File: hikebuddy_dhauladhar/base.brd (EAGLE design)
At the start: 75 x 40 mm, 119 parts, among them J1 MF-CON-MICROUSB-RIGHT, J2 GPS Port, J5 SOLDER_PAD_2, J9 47352-1001, U1 LTC3586EUFE-1#PBF, U2 MAX17260SETD+, U3 MF-DSC-SOT233-MMBT3904, U4 MF-DSC-SOT233-MMBT3904, U5 DRV2605LTDGSRQ1, U7 LSM303CTR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

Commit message: pulled up fault and EN to V_REG to fix startup bug
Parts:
- added C20: 1uF, MF_Passives:C0603
- added R16: 10K, MF_Passives:R0603
- moved C24 0.05 mm to (10.8, 19.2)
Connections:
- new net N$24: C20.P$2, R16.P$2, U1.18, U1.38
- net GND: now also C20.P$1
- net V_REG: now also R16.P$1; no longer U1.18
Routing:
- net N$24: track 0.00 -> 38.6 mm, vias 0 -> 2
- net EN_SDC: track 15.6 -> 17.0 mm
- net EN_GPS: track 14.0 -> 15.1 mm
- net SW4: track 72.1 -> 71.6 mm
- net SW3: track 59.2 -> 58.6 mm
- net VCC: track 235.5 -> 235.0 mm

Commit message: replace lsm303 with bmx160
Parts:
- removed C39: 10uF, SparkFun-Capacitors:C0603
- removed C40: 0.1uF, SparkFun-Capacitors:C0603
- removed R39: 750K, SparkFun-Resistors:R0603
- removed R44: 560K, SparkFun-Resistors:R0603
- removed R45: 100K, SparkFun-Resistors:R0603
- removed U7: LSM303CTR, LSM303CTR:LGA-12
- removed U9: LTC6991CDCB#TRMPBF, LTC6991CS6TRMPBF:DFN
- added C21: 10uF, SparkFun-Capacitors:C0603
- added U6: BMX160, BMX160:PQFN50P250X300X100-14N
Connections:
- removed net N$23: C40.2, U7.5
- removed net N$35: U$5.EXTCOMIN, U9.6
- removed net N$40: R39.1, U9.3
- removed net N$42: R44.2, R45.1, U9.2
- net ACCL1: now also J8.6; no longer U7.7
- net ACCL2: now also U6.4; no longer U7.12
- net ESP_FLASH: no longer J8.6
- net GND: now also C21.2, U6.1, U6.2, U6.3, U6.6, U6.7; no longer C39.2, C40.1, R39.2, R45.2, U7.6, U7.8, U9.4, U9.5, U9.7
- net I2C_SCL: now also U6.13; no longer U7.1
- net I2C_SDA: now also U6.14; no longer U7.4
- net MAGDRDY: now also U$5.EXTCOMIN; no longer U7.11
- net VCC: now also C21.1, U6.12, U6.5, U6.8; no longer C39.1, U7.10, U7.2, U7.3, U7.9
- net V_LCD: no longer R44.1, U9.1
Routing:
- net GND: track 505.3 -> 497.5 mm, vias 95 -> 94
- net N$42: track 5.21 -> 0.00 mm, vias 2 -> 0
- net VCC: track 235.0 -> 230.8 mm
- net N$35: track 4.03 -> 0.00 mm, vias 2 -> 0
- net MAGDRDY: track 50.8 -> 54.3 mm, vias 3 -> 5
- net ESP_FLASH: track 70.9 -> 67.4 mm
- net N$23: track 2.74 -> 0.00 mm, vias 1 -> 0
- net I2C_SDA: track 112.9 -> 111.2 mm
- net I2C_SCL: track 111.3 -> 109.8 mm
- net V_LCD: track 57.9 -> 56.6 mm
- net N$40: track 1.26 -> 0.00 mm
- net ACCL2: track 44.1 -> 43.0 mm
- net ACCL1: track 39.7 -> 39.2 mm
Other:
- board text added: "IO13"
- board text added: "IO14"
- board text added: "IO15"
- board text added: "IO33"
- board text removed: "GPIO0/ FLASH"
- board text removed: "GPIO13"
- board text removed: "GPIO14"
- board text removed: "GPIO15"

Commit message: fixed power, routed bmx160, changed and routed buttons; cs_v2_non_macrofab
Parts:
- S1, S2, S3, S4: value B3U-3000P -> EVQ-P4HB3B; device B3U-3000P:SW_B3U-3000P -> EVQ-P4HB3B:SW_EVQ-P4HB3B
- moved S4 14.7 mm to (53.7, 38.3)
- moved S2 13.5 mm to (39.5, 38.3)
- moved R33 1.96 mm to (54.4, 38.9), flipped to the top, turned to 0 degrees
- moved U6 1.00 mm to (45.0, 20.0)
- moved C21 0.99 mm to (44.8, 17.6)
- moved S1 0.83 mm to (53.7, 1.70)
- moved S3 0.71 mm to (25.6, 38.3)
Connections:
- net GND: now also S1.2, S1.3, S1.4, S2.2, S2.3, S2.4, S3.2, S3.3, S3.4, S4.2, S4.3, S4.4; no longer S1.1, S2.1, S3.1, S4.1
- net SW1: now also S1.1; no longer S1.2
- net SW2: now also S4.1; no longer S2.2
- net SW3: now also S3.1; no longer S3.2
- net SW4: now also S2.1; no longer S4.2
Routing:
- net GND: track 497.5 -> 526.5 mm, vias 94 -> 95
- net MAGDRDY: track 54.3 -> 41.4 mm, vias 5 -> 3
- net VCC: track 230.8 -> 241.6 mm
- net ESP_FLASH: track 67.4 -> 58.1 mm, vias 5 -> 3
- net SW3: track 58.6 -> 64.5 mm
- net ACCL2: track 43.0 -> 37.2 mm, vias 3 -> 1
- net SW2: track 89.0 -> 84.0 mm, vias 2 -> 3
- net I2C_SDA: track 111.2 -> 115.6 mm
- net ACCL1: track 39.2 -> 35.0 mm, vias 3 -> 2
- net I2C_SCL: track 109.8 -> 113.4 mm
- net SW1: track 68.1 -> 71.5 mm
- net N$33: track 27.5 -> 29.3 mm
- net SW4: track 71.6 -> 69.9 mm
- net V_LCD: track 56.6 -> 55.6 mm
- net N$32: track 27.9 -> 28.8 mm
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
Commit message: cs_v2_macrofab_sdc_version
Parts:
- removed J9: 47352-1001, 47352-1001:MOLEX_47352-1001
- added SD1: MF-MICROSD, MF_Connectors:MF-MICROSD
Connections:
- removed net N$19: J9.8
- removed net N$45: J9.1
- net 3V3_SDC: now also SD1.PIN4; no longer J9.4
- net GND: now also SD1.G0, SD1.G1, SD1.PIN6; no longer J9.6, J9.S1, J9.S2, J9.S3, J9.S4
- net SD_CLK: now also SD1.PIN5; no longer J9.5
- net SD_CS: now also SD1.PIN2; no longer J9.2
- net SD_MISO: now also SD1.PIN7; no longer J9.7
- net SD_MOSI: now also SD1.PIN3; no longer J9.3
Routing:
- net GND: track 526.5 -> 520.2 mm, vias 95 -> 94
- net SD_MISO: track 24.9 -> 23.1 mm
- net SD_CS: track 25.1 -> 23.5 mm
- net ESP_FLASH: track 58.1 -> 56.5 mm
- net SD_MOSI: track 22.9 -> 21.6 mm
- net 3V3_SDC: track 28.7 -> 27.4 mm
- net SD_CLK: track 26.5 -> 25.2 mm
- net EN_SDC: track 17.0 -> 18.1 mm
- net VCC: track 241.6 -> 242.5 mm

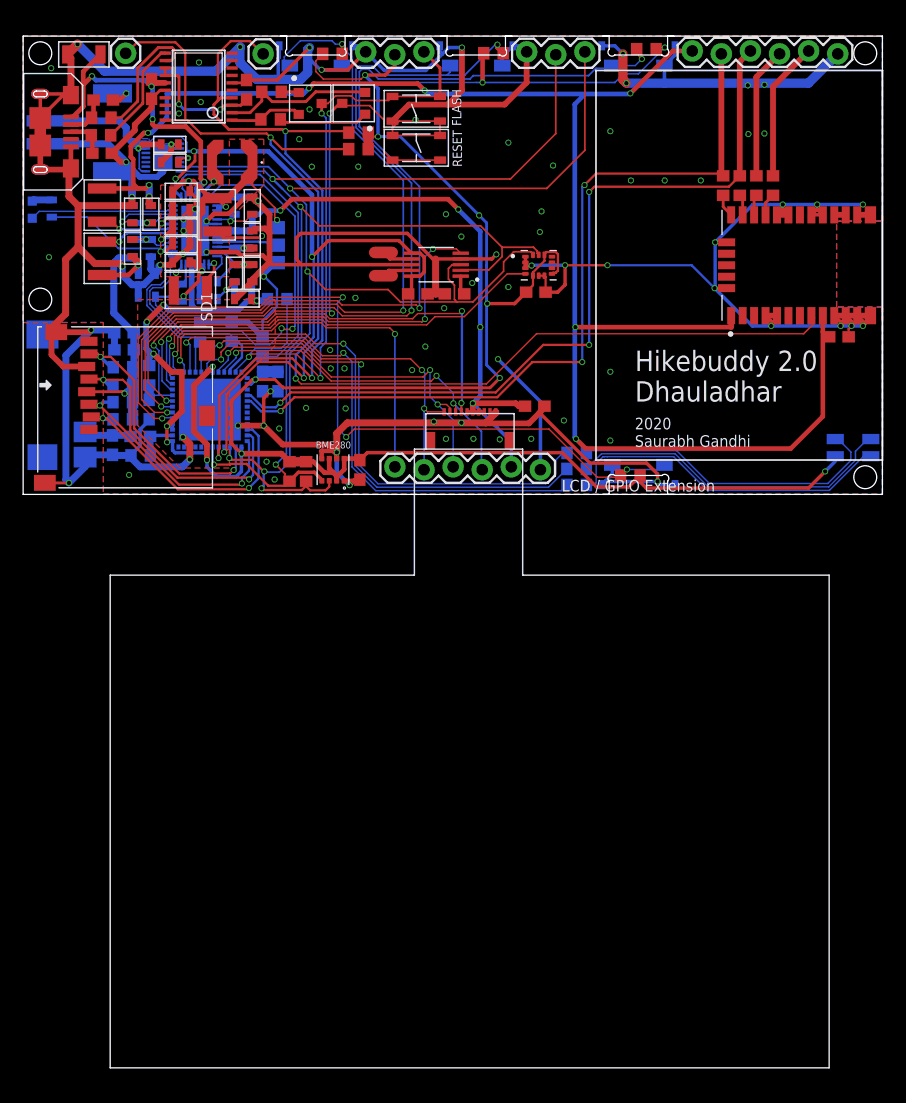
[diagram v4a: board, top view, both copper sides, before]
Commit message: reassigned input-only pins
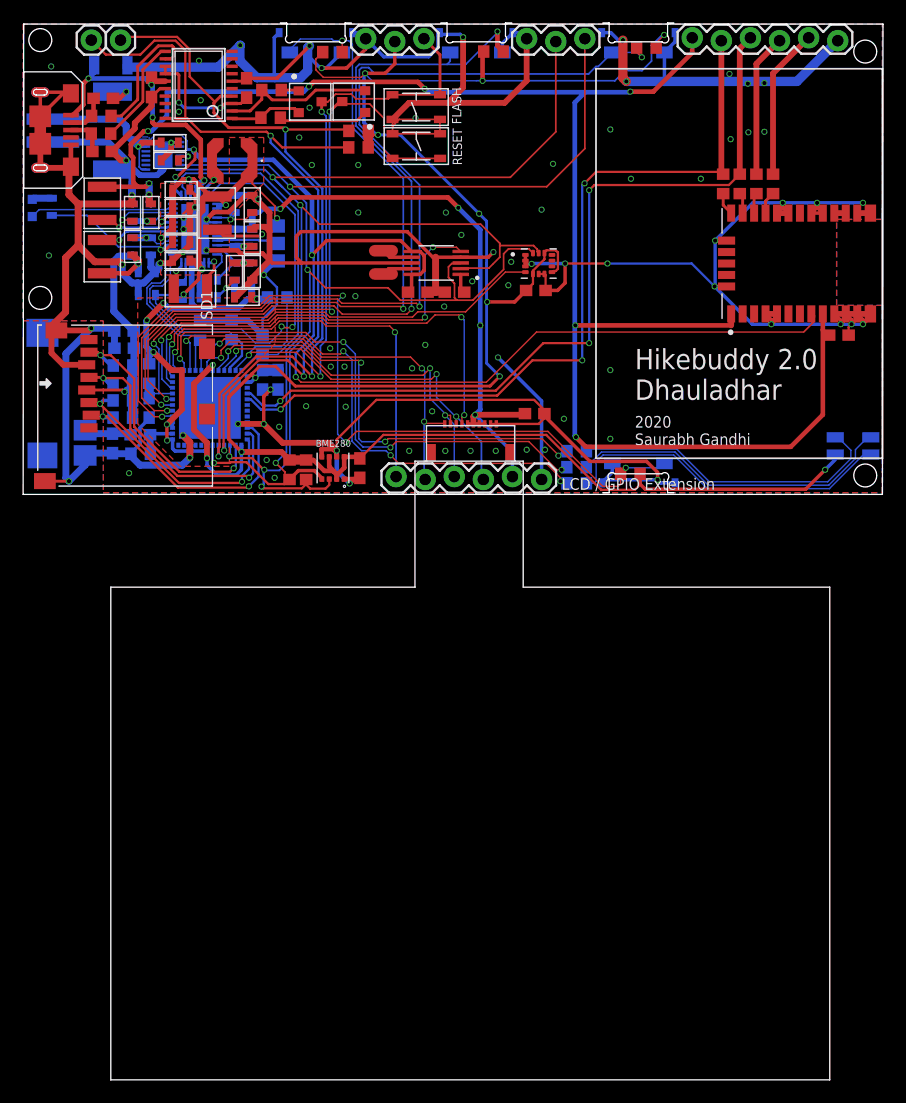
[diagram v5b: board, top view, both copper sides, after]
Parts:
- moved J7 12.5 mm to (8.50, 39.6)
- moved J6 3.21 mm to (5.95, 39.6)
- moved C9 2.53 mm to (7.65, 37.5), flipped to the bottom
- moved S2 1.15 mm to (39.5, 39.5)
- moved S3 1.15 mm to (25.6, 39.5)
- moved S4 1.15 mm to (53.7, 39.5)
- moved J2 1.15 mm to (71.1, 39.6)
- moved J3 1.15 mm to (44.0, 39.6)
- moved J4 1.15 mm to (29.9, 39.6)
- moved U$5 1.05 mm to (39.0, 0.90)
- moved J8 0.86 mm to (45.2, 1.30)
- moved C19 0.65 mm to (44.6, 7.05)
- moved C10 0.15 mm to (20.0, 25.4)
- moved C12 0.15 mm to (13.8, 26.6)
- moved C13 0.15 mm to (11.2, 24.6)
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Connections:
- net ACCL1 renamed GPIO_EXT
- removed net ACCL2: ESP32-PICO-D4.12, U6.4
- removed net MAGDRDY: ESP32-PICO-D4.10, U$5.EXTCOMIN
- new net BMX_INT: ESP32-PICO-D4.10, U6.4
- new net LCD_EXTCOMM: ESP32-PICO-D4.12, U$5.EXTCOMIN
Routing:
- net MAGDRDY: track 41.4 -> 0.00 mm, vias 3 -> 0
- net LCD_EXTCOMM: track 0.00 -> 39.7 mm, vias 0 -> 3
- net BMX_INT: track 0.00 -> 39.4 mm, vias 0 -> 1
- net ACCL2: track 37.2 -> 0.00 mm, vias 1 -> 0
- net VCC: track 242.5 -> 250.2 mm
- net ESP_RX: track 68.0 -> 71.7 mm
- net LED1: track 45.6 -> 42.0 mm, vias 2 -> 4
- net ESP_TX: track 64.0 -> 67.1 mm
- net V_USB: track 29.0 -> 26.8 mm
- net LED3: track 48.9 -> 46.9 mm, vias 2 -> 4
- net SW1: track 71.5 -> 73.4 mm
- net LED2: track 47.6 -> 46.2 mm, vias 2 -> 4
- net I2C_SDA: track 115.6 -> 116.9 mm
- net 3V3_GPS: track 147.0 -> 148.2 mm
- net LCD_CLK: track 32.8 -> 33.8 mm
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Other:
- board size 75 x 40 mm -> 75 x 41 mm
- board text added: "IO32"
- board text removed: "IO14"

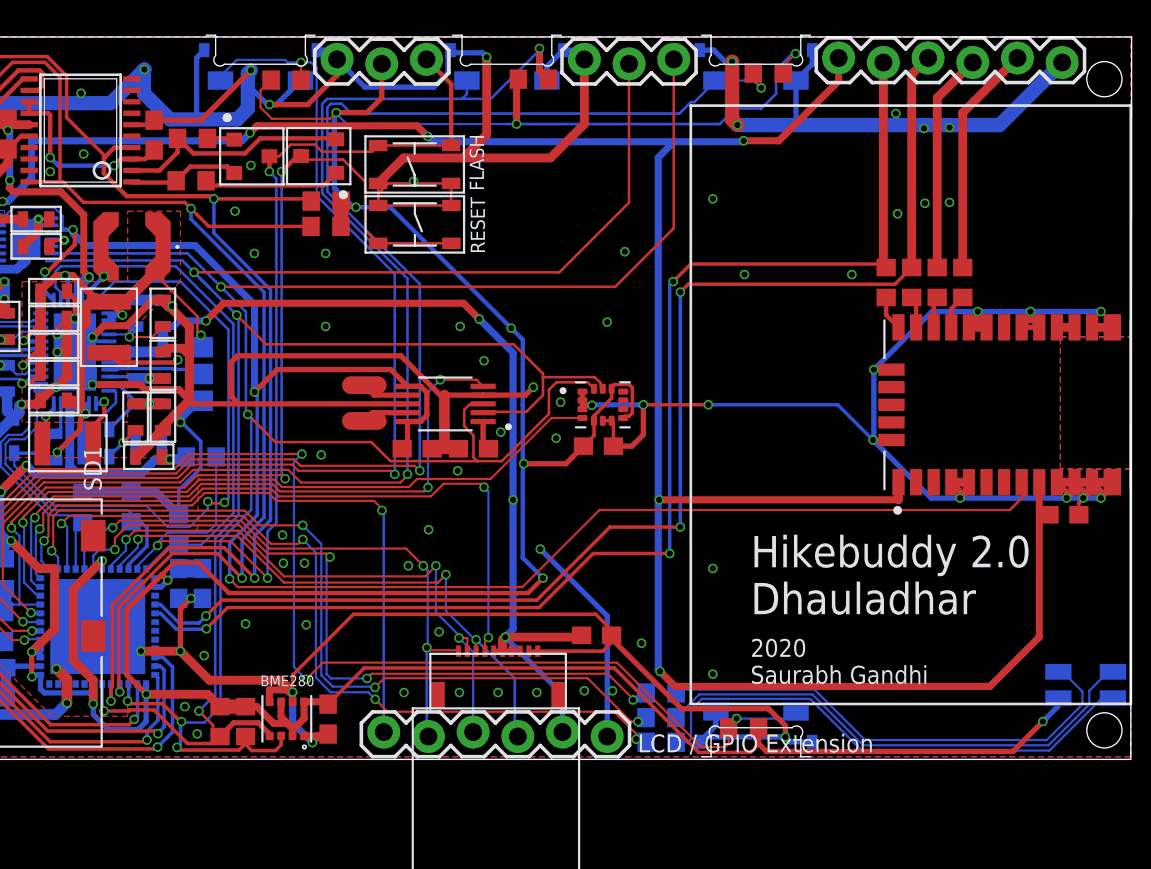
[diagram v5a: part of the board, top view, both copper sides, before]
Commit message: export cam files
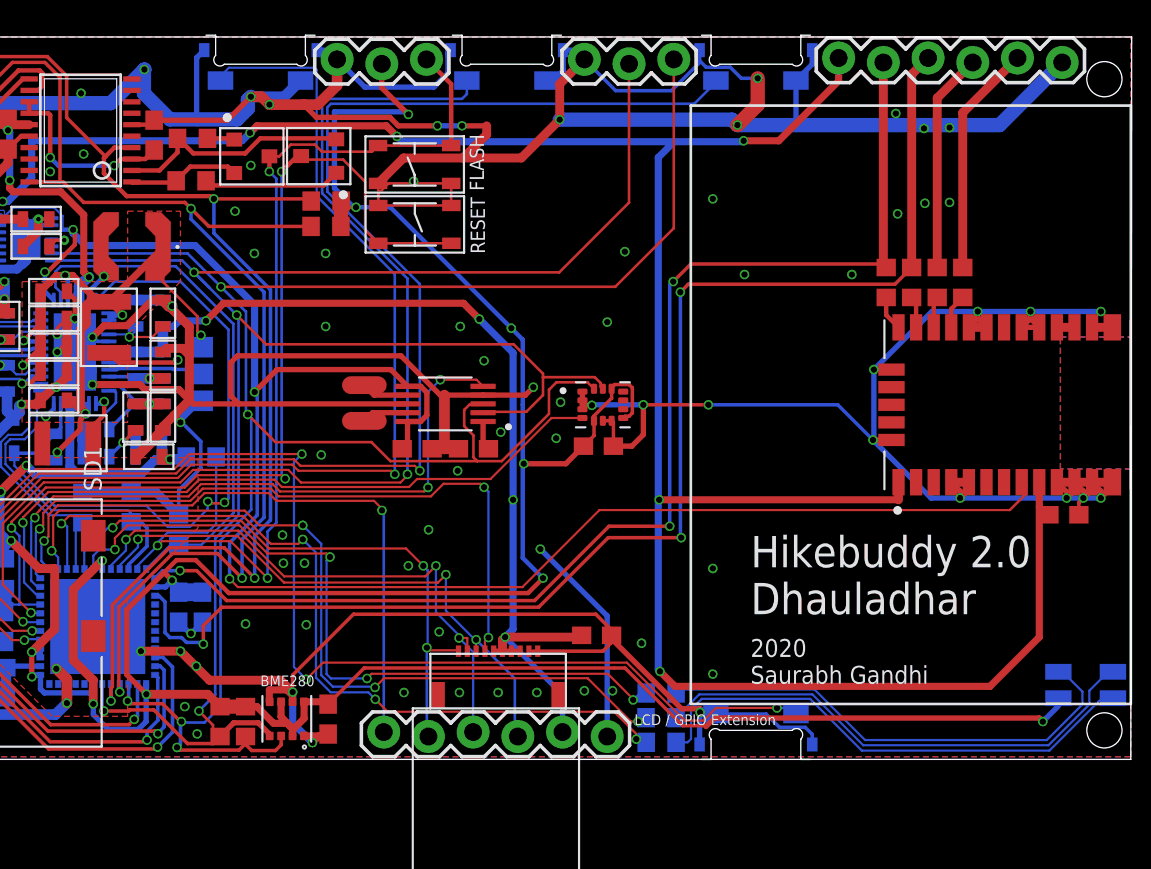
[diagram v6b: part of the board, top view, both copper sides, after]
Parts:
- removed R32, R33, R34, R35: 10k, SparkFun-Resistors:R0603
- moved C38 1.35 mm to (20.9, 8.65)
- moved C8 1.35 mm to (22.2, 8.65)
- moved S1 0.15 mm to (53.7, 1.70)
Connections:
- net GPS_RX: now also ESP32-PICO-D4.25; no longer ESP32-PICO-D4.29
- net GPS_TX: now also ESP32-PICO-D4.27; no longer ESP32-PICO-D4.28
- net NC2: now also ESP32-PICO-D4.28; no longer ESP32-PICO-D4.30
- net NC3: now also ESP32-PICO-D4.29; no longer ESP32-PICO-D4.31
- net NC4: now also ESP32-PICO-D4.30; no longer ESP32-PICO-D4.25
- net NC5: now also ESP32-PICO-D4.31; no longer ESP32-PICO-D4.27
- net SW1: no longer R32.1
- net SW2: no longer R33.1
- net SW3: no longer R34.1
- net SW4: no longer R35.1
- net VCC: no longer R32.2, R33.2, R34.2, R35.2
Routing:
- net VCC: track 250.2 -> 210.4 mm, vias 18 -> 16
- net GND: track 520.5 -> 535.2 mm, vias 94 -> 96
- net SW4: track 70.9 -> 63.3 mm, vias 3 -> 2
- net SW2: track 84.1 -> 79.9 mm, vias 3 -> 2
- net GPS_TX: track 71.9 -> 75.2 mm
- net SW1: track 73.4 -> 71.8 mm
- net SW3: track 63.7 -> 62.3 mm, vias 3 -> 2
- net V_REG: track 56.0 -> 57.2 mm
- net GPS_RX: track 71.3 -> 70.2 mm

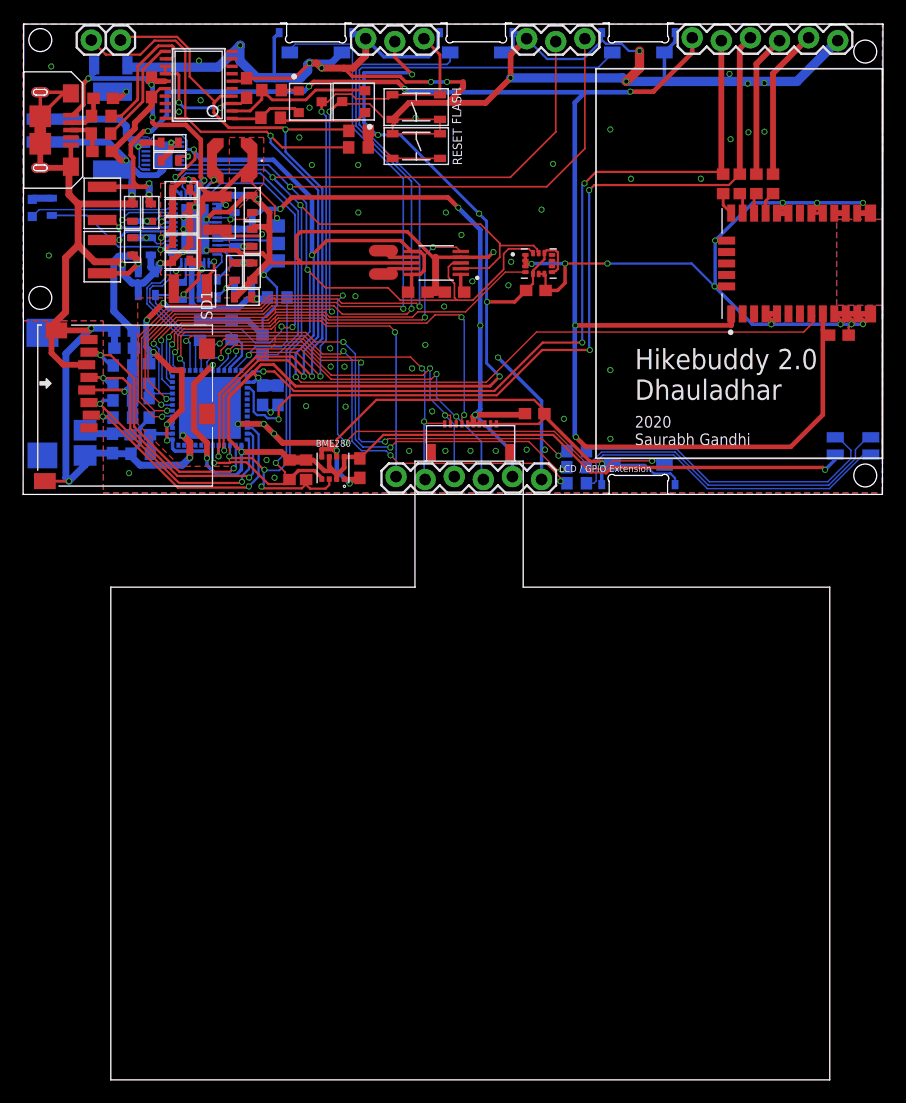
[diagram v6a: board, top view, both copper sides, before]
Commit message: rerouted traces close to milling; moved milling layer to dimension
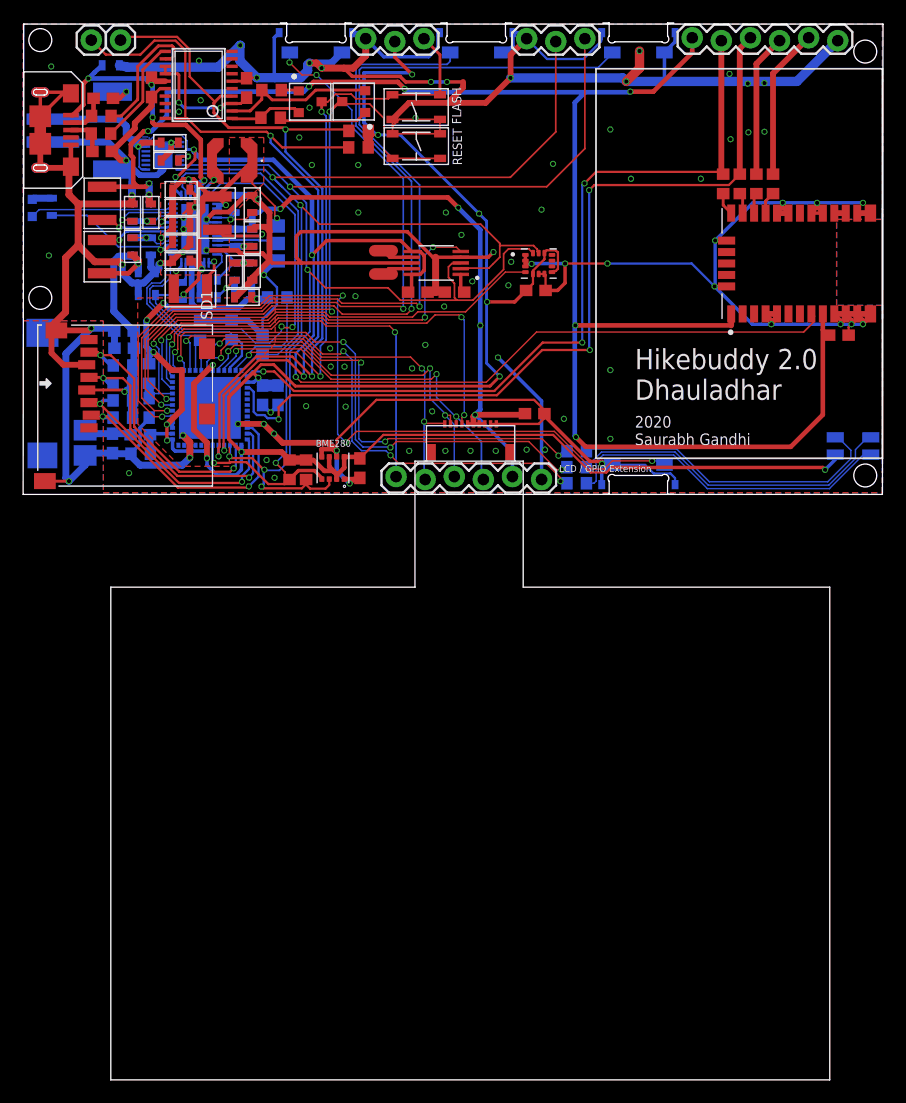
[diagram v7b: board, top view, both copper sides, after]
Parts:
- BATTERY1: value (none) -> S2B-PH-SM4-TB(LF)(SN)
- C9: device MF_Passives:C1206 -> MF_Passives:C0603
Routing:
- net GND: track 535.2 -> 526.9 mm, vias 96 -> 97
- net SW3: track 62.3 -> 58.6 mm, vias 2 -> 4
- net V_REG: track 57.2 -> 56.4 mm

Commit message: minor tweak
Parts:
- added TP1, TP2: TEST-POINT2, SparkFun-Connectors:PAD.02X.02
- C20: value 1uF -> 0.1uF
- R16: value 10K -> 1K
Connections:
- removed net HAP_EN: ESP32-PICO-D4.11, U5.5
- new net N$19: TP2.P$1, U1.18
- net GND: now also J2.3; no longer J2.1
- net GPS_RESET: now also J2.1; no longer J2.2
- net GPS_SAFEBOOT: now also J2.2; no longer J2.3
- net N$24: now also TP1.P$1; no longer U1.18
- net V_BAT: now also U5.5
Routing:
- net HAP_EN: track 36.8 -> 0.00 mm, vias 3 -> 0
- net GND: track 526.9 -> 521.2 mm
- net V_BAT: track 118.8 -> 123.3 mm, vias 5 -> 7
- net N$19: track 0.00 -> 2.54 mm
- net GPS_SAFEBOOT: track 12.5 -> 13.8 mm
- net GPS_RESET: track 13.2 -> 14.0 mm
